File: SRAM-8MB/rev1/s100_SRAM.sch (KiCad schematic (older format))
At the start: 123 parts, among them P1 S100_MALE, P34 CONN_1, P35 CONN_1, SW1 DIPS_08, SW2 DIPS_08, SW3 DIPS_08, SW4 DIPS_08, U1 LDO_REG_7805, U10 74LS01, U11 74LS85, U12 ^^74LS11, U13 ^^74LS11, U14 74LS08, U15 74LS02, U16 74LS85, U18 74LS32, U19 74LS245, U2 74LS244, U20 74HC00, U21 SRAM_512KB, U22 74LS245, U23 74LS244, U24 74LS244, U25 74LS32, U26 SRAM_512KB, U27 74LS165, U29 SRAM_512KB, U3 74LS138, U30 ^^74LS27, U31 74LS245, U32 SRAM_512KB, U33 SRAM_512KB, U34 SRAM_512KB, U35 SRAM_512KB, U36 SRAM_512KB, U37 SRAM_512KB, U38 SRAM_512KB, U39 SRAM_512KB, U4 74LS138, U40 SRAM_512KB, U41 SRAM_512KB, U42 SRAM_512KB, U43 SRAM_512KB, U44 SRAM_512KB, U5 74LS85, U6 74LS85, U7 74LS85, U8 74LS85

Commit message: SRAM-8MB rev1: schematic and layout update (C38 removed)
Source: S100 8MB SRAM proto1/BACKUPS/20032014 1941
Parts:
- removed C38: 0.1 uF, C2, symbol C
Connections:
- wire segments 1206 -> 1204
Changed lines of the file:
@@
 Connection ~ 29400 13900
 Wire Wire Line
-	-3700 5100 -750 5100
-Wire Wire Line
 	-4900 5200 -5500 5200
 Wire Wire Line
@@
 $EndComp
 $Comp
-L C C38
-U 1 1 4B37DA08
-P 23550 3100
-AR Path="/FFFFFFFF4B37DA08" Ref="C38"  Part="1"
-AR Path="/4B37DA08" Ref="C38"  Part="1"
-AR Path="/94B37DA08" Ref="C38"  Part="1"
-AR Path="/A4B37DA08" Ref="C38"  Part="1"
-AR Path="/6FE901F74B37DA08" Ref="C38"  Part="1"
-AR Path="/402755814B37DA08" Ref="C38"  Part="1"
-AR Path="/3FEFFFFF4B37DA08" Ref="C38"  Part="1"
-AR Path="/4030AAC04B37DA08" Ref="C38"  Part="1"
-AR Path="/FFFFFFF04B37DA08" Ref="C38"  Part="1"
-AR Path="/5AD7153D4B37DA08" Ref="C38"  Part="1"
-AR Path="/A84B37DA08" Ref="C38"  Part="1"
-AR Path="/14B37DA08" Ref="C38"  Part="1"
-AR Path="/6FF0DD404B37DA08" Ref="C38"  Part="1"
-AR Path="/23D9304B37DA08" Ref="C38"  Part="1"
-AR Path="/23D8D44B37DA08" Ref="C38"  Part="1"
-AR Path="/4031DDF34B37DA08" Ref="C38"  Part="1"
-AR Path="/3FE88B434B37DA08" Ref="C38"  Part="1"
-AR Path="/4032778D4B37DA08" Ref="C38"  Part="1"
-AR Path="/403091264B37DA08" Ref="C38"  Part="1"
-AR Path="/403051264B37DA08" Ref="C38"  Part="1"
-AR Path="/4032F78D4B37DA08" Ref="C38"  Part="1"
-AR Path="/403251264B37DA08" Ref="C38"  Part="1"
-AR Path="/4032AAC04B37DA08" Ref="C38"  Part="1"
-AR Path="/4030D1264B37DA08" Ref="C38"  Part="1"
-AR Path="/4031778D4B37DA08" Ref="C38"  Part="1"
-AR Path="/3FEA24DD4B37DA08" Ref="C38"  Part="1"
-AR Path="/2600004B37DA08" Ref="C38"  Part="1"
-AR Path="/6FE934E34B37DA08" Ref="C38"  Part="1"
-AR Path="/773F65F14B37DA08" Ref="C38"  Part="1"
-AR Path="/773F8EB44B37DA08" Ref="C38"  Part="1"
-AR Path="/23C9F04B37DA08" Ref="C38"  Part="1"
-AR Path="/24B37DA08" Ref="C38"  Part="1"
-AR Path="/23BC884B37DA08" Ref="C38"  Part="1"
-AR Path="/DC0C124B37DA08" Ref="C38"  Part="1"
-AR Path="/23C34C4B37DA08" Ref="C38"  Part="1"
-AR Path="/23CBC44B37DA08" Ref="C38"  Part="1"
-AR Path="/23C6504B37DA08" Ref="C38"  Part="1"
-AR Path="/39803EA4B37DA08" Ref="C38"  Part="1"
-AR Path="/D058A04B37DA08" Ref="C38"  Part="1"
-AR Path="/1607D44B37DA08" Ref="C38"  Part="1"
-AR Path="/D1C3804B37DA08" Ref="C38"  Part="1"
-AR Path="/23D70C4B37DA08" Ref="C38"  Part="1"
-AR Path="/2104B37DA08" Ref="C38"  Part="1"
-F 0 "C38" H 23600 3200 50  0000 L CNN
-F 1 "0.1 uF" H 23600 3000 50  0000 L CNN
-F 2 "C2" H 23550 3100 60  0000 C CNN
-F 3 "" H 23550 3100 60  0001 C CNN
-	1    23550 3100
-	1    0    0    -1
-$EndComp
-$Comp
 L C C39
 U 1 1 4B37DA03
@@
 	18600 -8900 18050 -8900
 Wire Wire Line
-	18050 -10600 18050 -6850
-Wire Wire Line
 	18050 -10600 19750 -10600
 $Comp
@@
 	18150 -6750 17250 -6750
 Connection ~ 18150 -8800
-Wire Wire Line
-	18050 -6850 17250 -6850
-Connection ~ 18050 -8900
 Text Notes 16550 -6800 0    60   ~ 0
 xx\nA23\nA22\nA21
@@
 	18150 -17250 18150 -13500
 Wire Wire Line
-	17950 -17350 17950 -9400
+	17950 -17350 17950 -9300
 Wire Wire Line
 	17950 -17350 19750 -17350
@@
 Connection ~ 1350 5150
 Wire Wire Line
-	17950 -9400 18600 -9400
-Wire Wire Line
 	18150 -13500 17500 -13500
 Wire Wire Line
@@
 Text Label 47750 9450 0    60   ~ 0
 ~RAMCS4
+Wire Wire Line
+	18050 -8900 18050 -10600
+Wire Wire Line
+	17950 -9300 18600 -9300
 $EndSCHEMATC

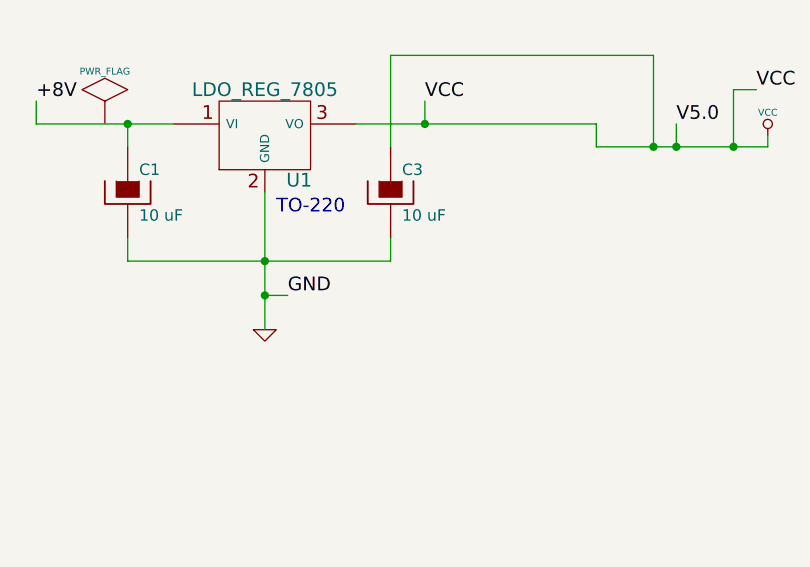
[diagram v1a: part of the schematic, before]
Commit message: SRAM-8MB rev1: routed board
Source: S100 8MB SRAM proto1/BACKUPS/20032014 2037
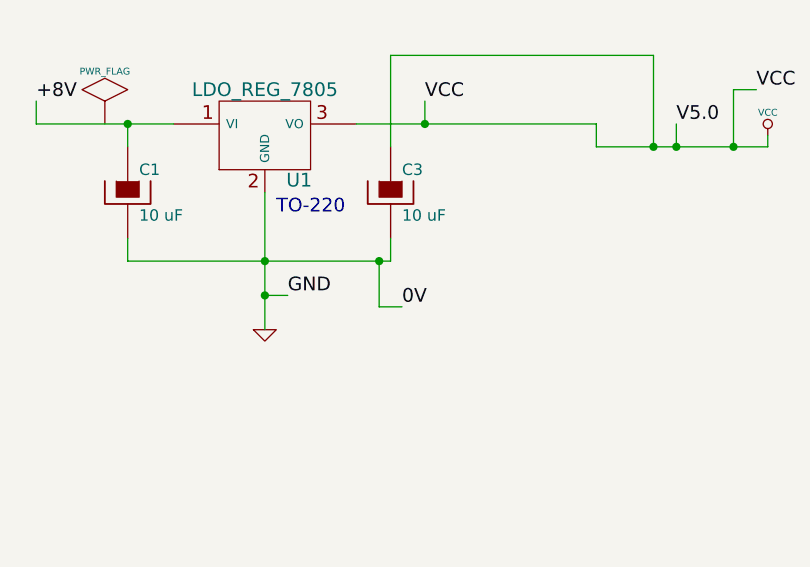
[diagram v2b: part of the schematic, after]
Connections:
- wire segments 1204 -> 1206
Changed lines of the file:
@@
 Wire Wire Line
 	17950 -9300 18600 -9300
+Text Label 28400 6100 0    60   ~ 0
+0V
+Wire Wire Line
+	28400 6100 28300 6100
+Wire Wire Line
+	28300 6100 28300 5900
+Connection ~ 28300 5900
 $EndSCHEMATC

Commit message: SRAM-8MB rev1: logo, BOM and fabrication gerbers
Source: S100 8MB SRAM proto1/ (working folder).
Dated by the board and gerbers (2014-03-24). The schematic in this folder was re-saved on 2014-04-07; that save is identical to its .bak and has the same parts as the 2014-03-24 netlist, so it is included here.
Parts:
- added unit 4 of U25
- added U45: LOGO_S100_SRAM_8MB, symbol LOGO_S100_SRAM_8MB
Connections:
- net labels added: B, BOARD_SELECT*
- net labels removed: BOARD_RAM_SELECT, BOARD_RAM_SELECT*, LOWER_SELECT, LOWER_SELECT*
- wire segments 1206 -> 1210
- no-connect marks 44 -> 43
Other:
- note added: "A* active low MEM READ\n"
- note added: "B* active low data BRIDGE\n"
- note added: "B* active low\n ODD address MEM WRITE\n EVEN address MEM READ\n"
- note added: "B->A"
- note added: "C* active low MEM WRITE\n"
- note added: "D* active low ODD bank OE\n"
- note added: "Data INPUT\n from S100 Bus\n"
- note added: "Data OUTPUT\n to S100 Bus\n"
- note added: "E* active low EVEN bank OE\n"
- note added: "F* active low ODD bank WE\n"
- note added: "G* active low EVEN bank WE\n"
- note added: "pin 65 S100 bus\nMemory Request (active low)\n~MEMRQ\n"
- moved on the sheet: C1, C3, JP1, JP2, JP3, JP8, P1, P34, P35, RR1, RR2, RR3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
